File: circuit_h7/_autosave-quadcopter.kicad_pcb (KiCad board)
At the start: 4 copper layers, 37.5 x 37.5 mm, 109 parts, among them J1 Conn_01x04_Male, J10 Conn_01x01_Female, J11 Conn_01x04_Male, J12 Conn_01x04_Male, J13 Conn_01x01_Female, J14 Conn_01x01_Female, J15 Conn_01x01_Female, J16 Conn_01x01_Female, J17 Conn_01x01_Female, J18 USB_C_Receptacle_USB2.0, J19 Conn_01x08_Male, J2 Conn_01x01_Female, J21 Conn_01x01_Female, J22 Conn_01x01_Female, J23 Conn_01x01_Female, J24 Conn_01x01_Female, J25 Conn_01x01_Female, J26 Conn_01x01_Female, J28 Conn_01x01_Female, J29 Conn_01x01_Female, J3 Conn_01x01_Female, J30 Conn_01x01_Female, J31 Conn_01x01_Female, J32 Conn_01x01_Female, J33 Conn_01x01_Female, J37 Conn_01x01_Female, J4 Conn_01x01_Female, J40 Conn_01x01_Female, J41 Conn_01x01_Female, J42 Conn_01x01_Female, J43 Conn_01x01_Female, J44 Conn_01x01_Female, J45 Conn_01x01_Female, J47 Conn_01x01_Female, J48 Conn_01x01_Female, J49 Conn_01x01_Female, J5 Conn_Coaxial, J50 Conn_01x01_Female, J6 Conn_01x06_Male, J7 Conn_01x01_Female, J8 Conn_01x01_Female, J9 Conn_01x01_Female, SW1 SW_DIP_x01, U1 STM32H723VGH6, U2 ICM-42605, U3 DPS310, U4 3V3, U5 EUP3458 1.2A, 30V max input, 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, U6 2450FM07D0034T, U7 W25Q80DVUXIE TR (16M), U8 SX1281, U9 5v, 500mA, Y1 16M, Y2 52Mhz, 12pF

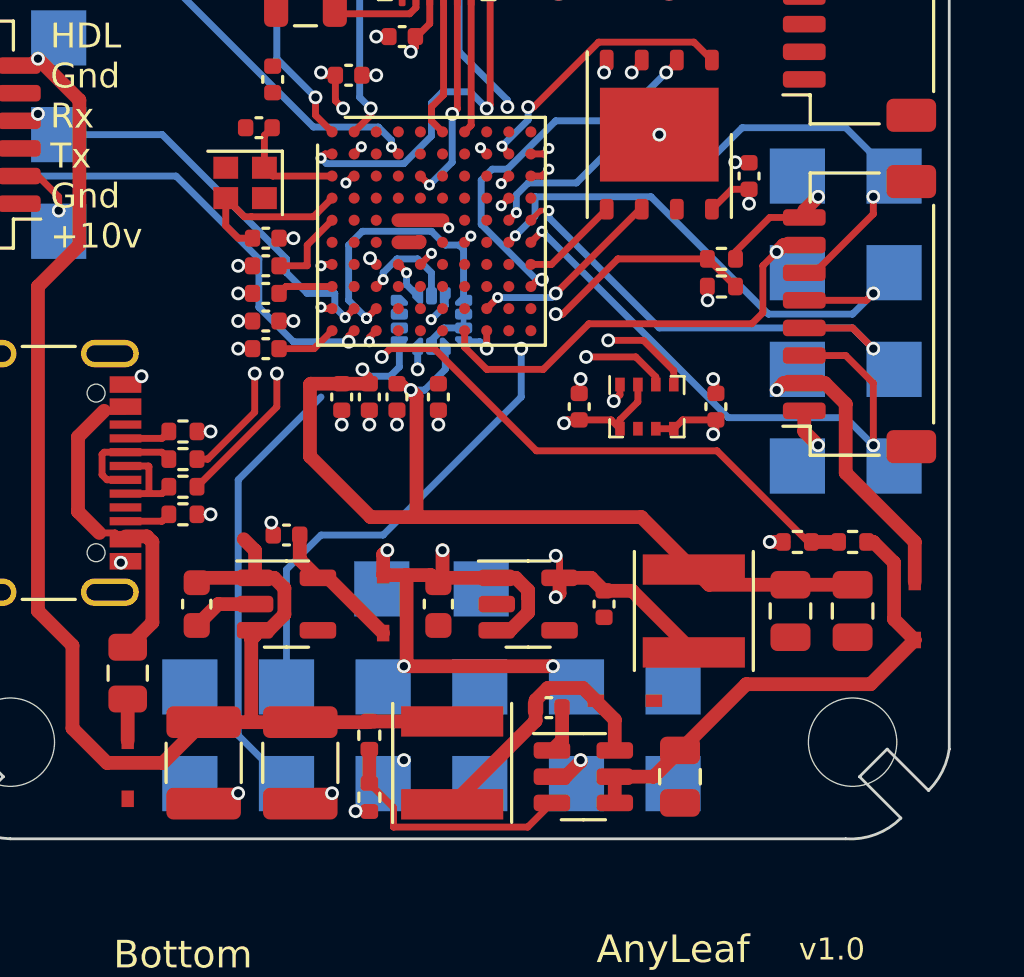
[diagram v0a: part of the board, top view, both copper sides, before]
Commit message: Updated to Django 4.0
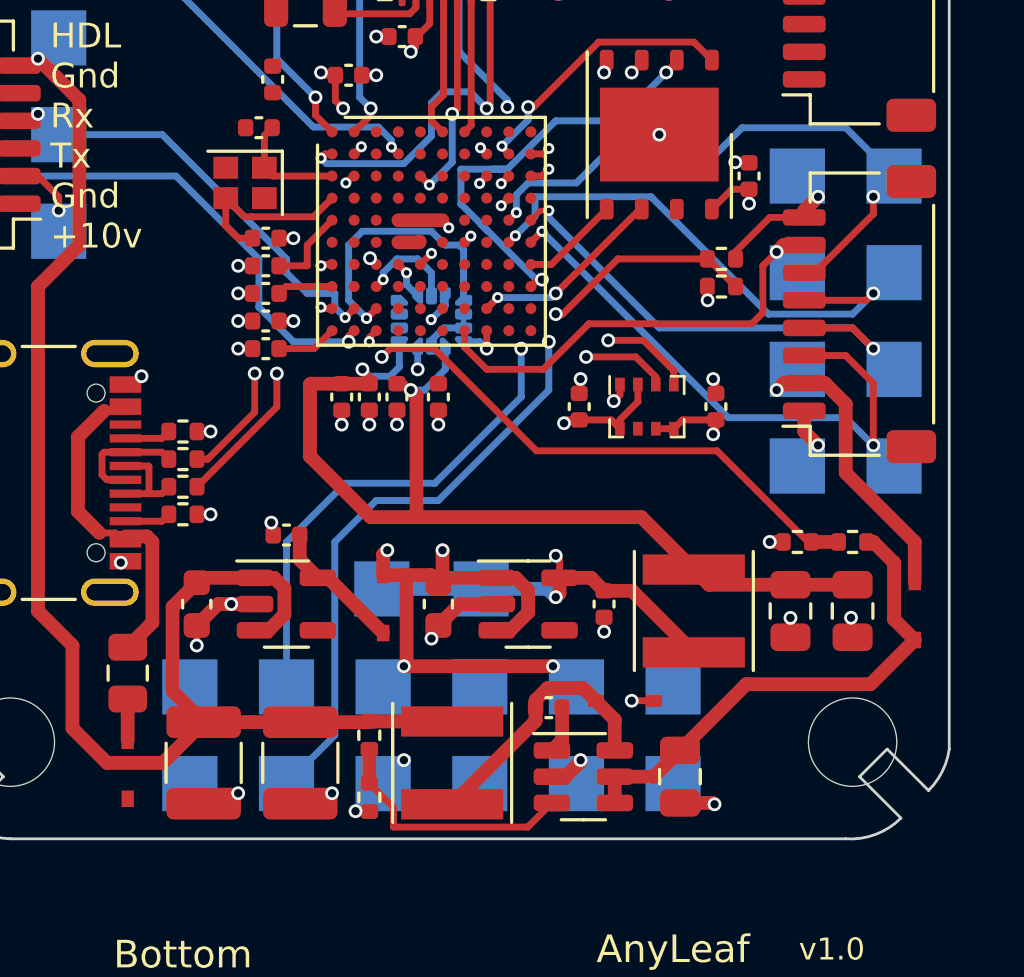
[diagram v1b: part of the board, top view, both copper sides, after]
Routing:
- net /UART4_TX: track 16.0 -> 31.4 mm, vias 0 -> 2
- net GND: track 33.7 -> 41.5 mm, vias 44 -> 52
- net +3V3: track 30.7 -> 37.1 mm
- net /MISO_2: track 14.1 -> 16.2 mm
- net /SDA2: track 29.6 -> 28.5 mm
- net +10V: track 52.3 -> 53.2 mm
- net /USB_DN: track 24.9 -> 24.2 mm
- net /UART4_RX: track 25.7 -> 26.3 mm

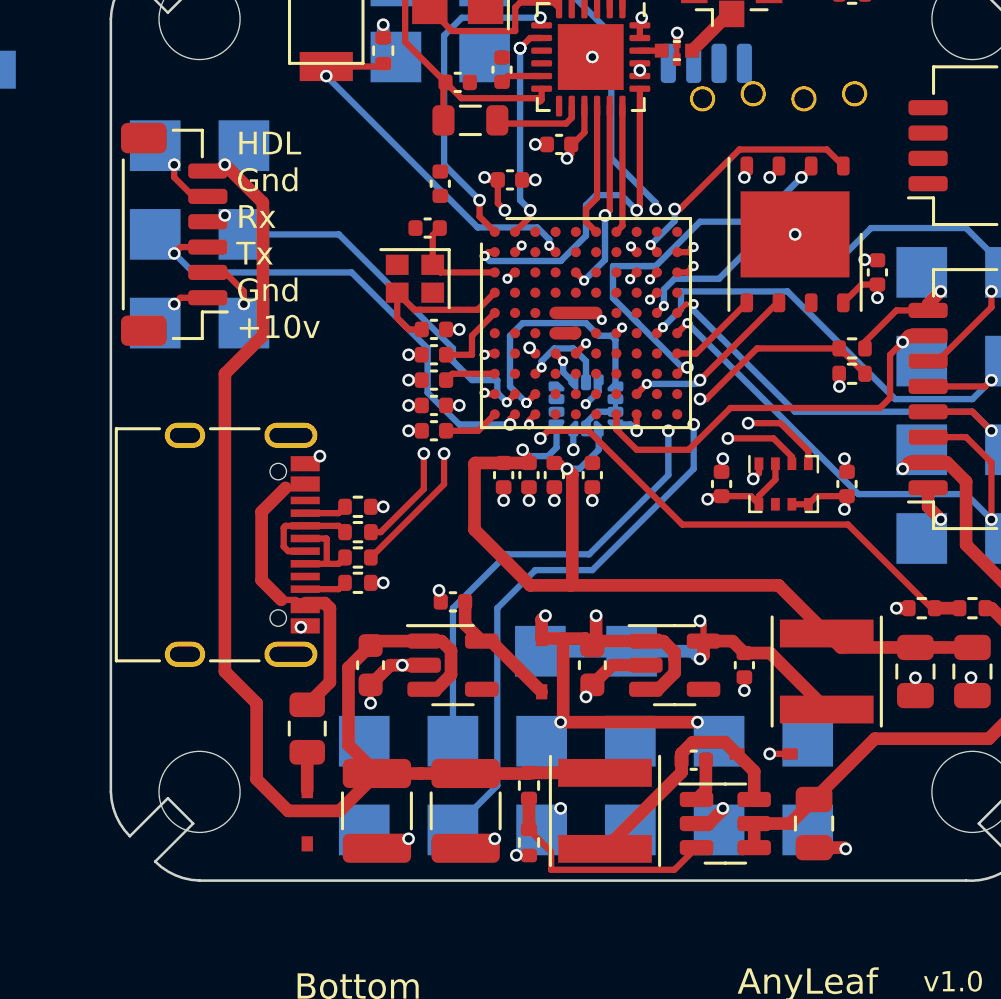
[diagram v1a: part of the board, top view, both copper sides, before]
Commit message: More work on board. Removed motor args from set power fns
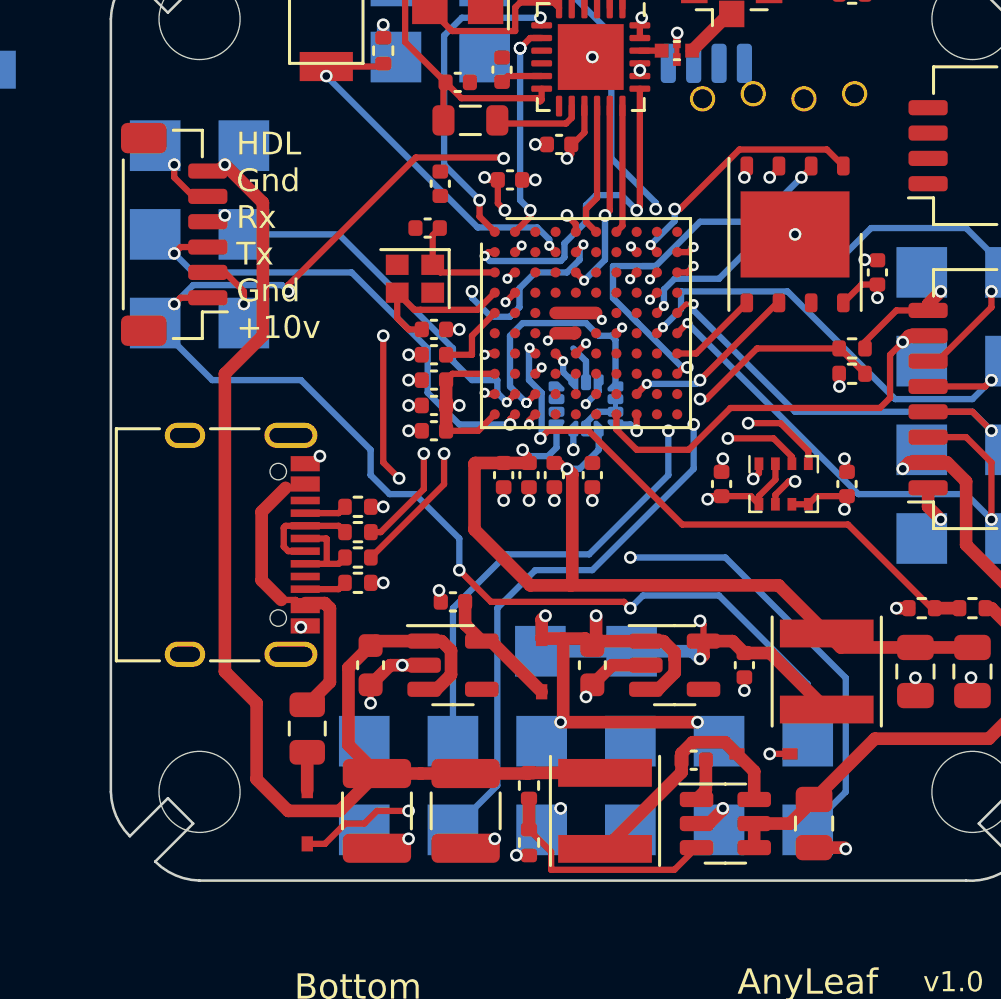
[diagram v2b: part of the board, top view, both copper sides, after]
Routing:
- net /UART1_RX: track 1.43 -> 57.6 mm, vias 1 -> 6
- net /UART1_TX: track 0.00 -> 44.9 mm, vias 0 -> 5
- net +5V: track 19.0 -> 31.0 mm, vias 4 -> 5
- net /BATT_DIV: track 19.9 -> 23.7 mm
- net /SCK_1: track 3.61 -> 1.90 mm
- net GND: track 41.5 -> 42.9 mm, vias 52 -> 53
- net +3V3: track 37.1 -> 38.5 mm, vias 13 -> 15

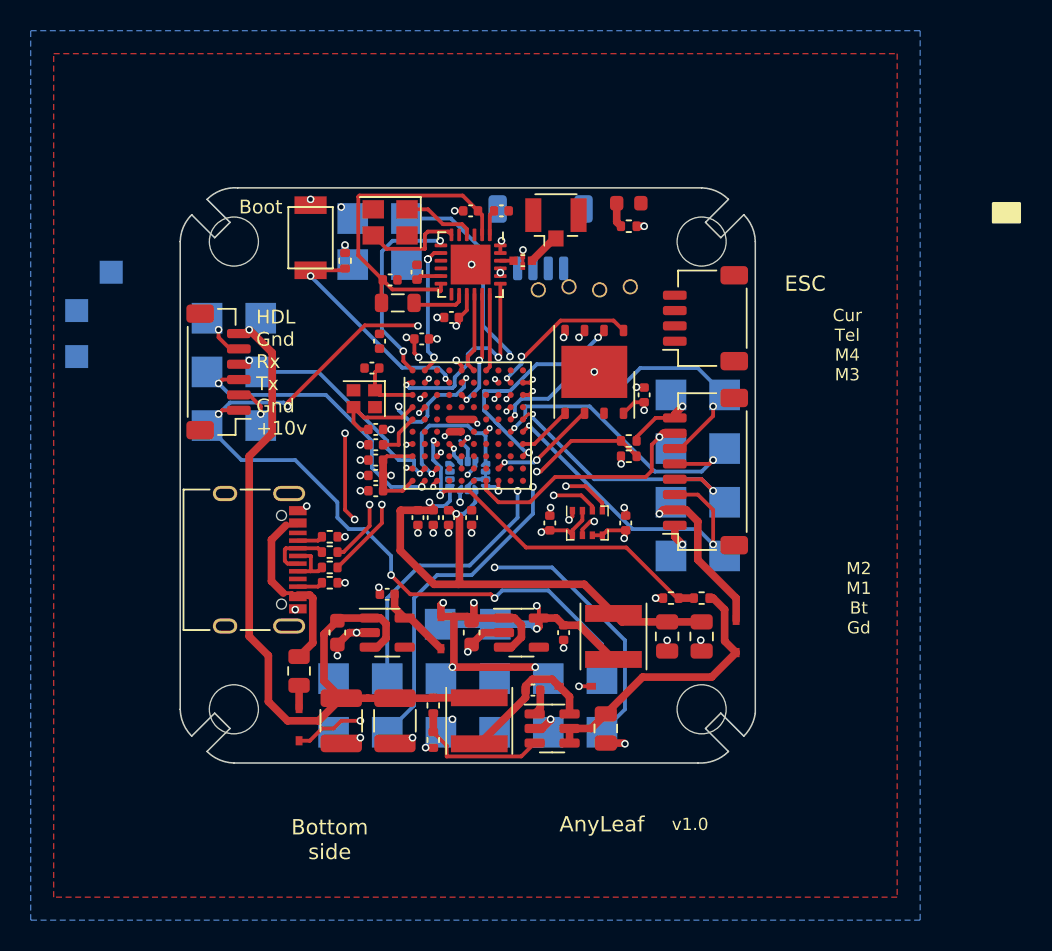
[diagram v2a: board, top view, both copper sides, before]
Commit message: Started switch to PID setup where starting point is prev control settings; no 0
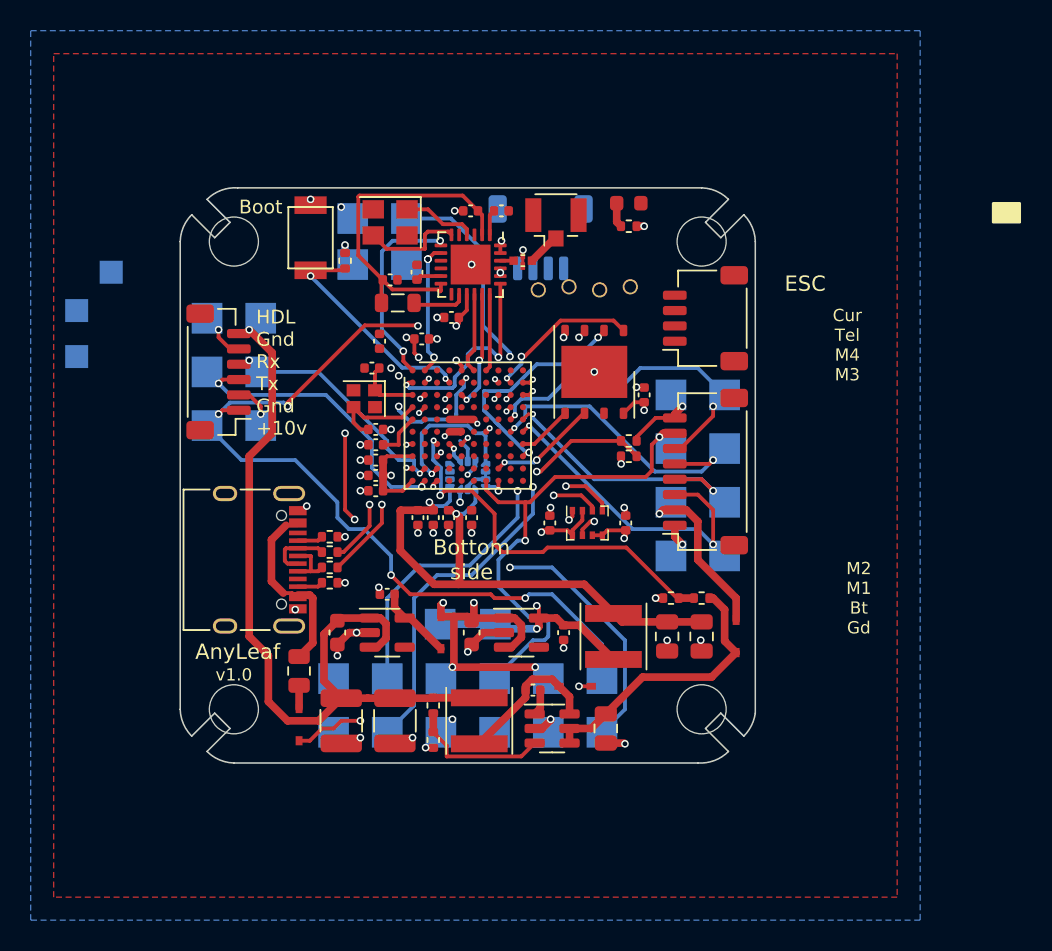
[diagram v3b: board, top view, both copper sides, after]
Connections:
- J14 pad 1: /UART5_RX -> /UART8_RX
- J2 pad 1: /UART5_TX -> /UART8_TX
- U1 pad C4: unconnected-(U1-PadC4) -> /UART8_TX
- U1 pad D4: unconnected-(U1-PadD4) -> /UART8_RX
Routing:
- net /UART3_RX: track 16.1 -> 32.4 mm, vias 1 -> 2
- net /UART8_TX: track 0.00 -> 5.55 mm, vias 0 -> 2
- net /UART8_RX: track 0.00 -> 4.36 mm, vias 0 -> 2
- net +3V3: track 38.5 -> 40.8 mm
- net /BATT_DIV: track 23.7 -> 25.1 mm
- net /UART1_TX: track 44.9 -> 45.6 mm
- net /USB_DP: track 23.2 -> 23.9 mm
